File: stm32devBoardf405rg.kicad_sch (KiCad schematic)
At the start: 25 parts, among them Q1 AO3401A, SW1 SW_SPDT, U1 STM32F405RGT6, Y1 16MZ

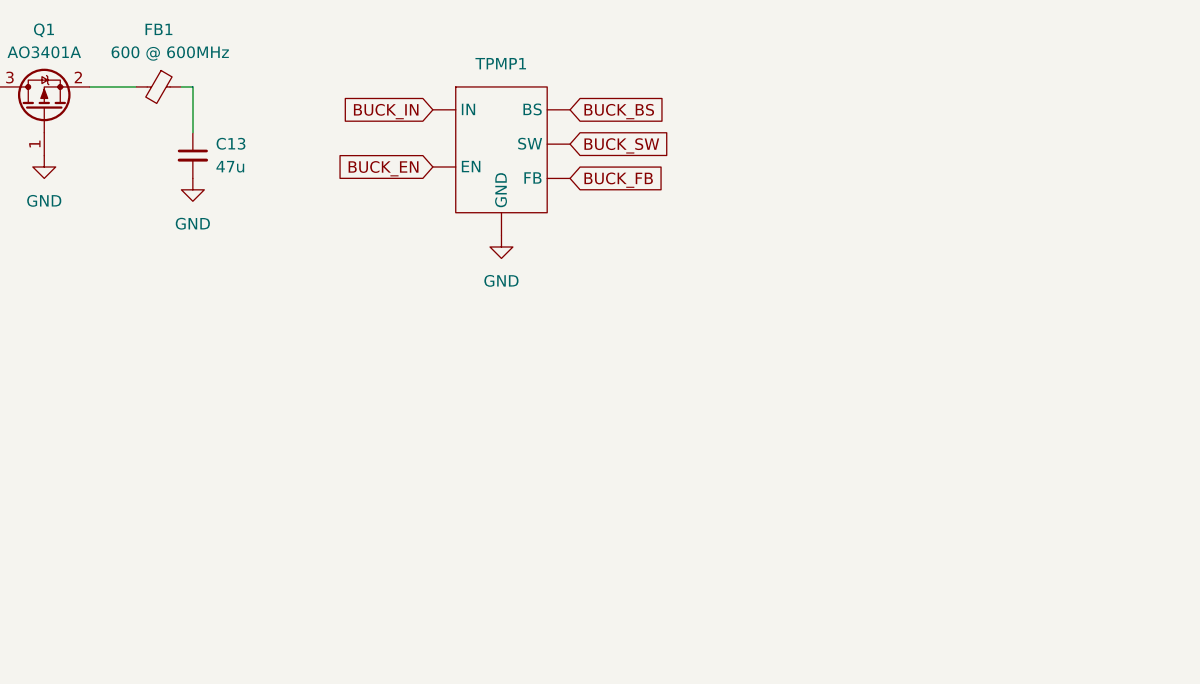
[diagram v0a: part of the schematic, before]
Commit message: added buck regulator TPMP2359 power supply
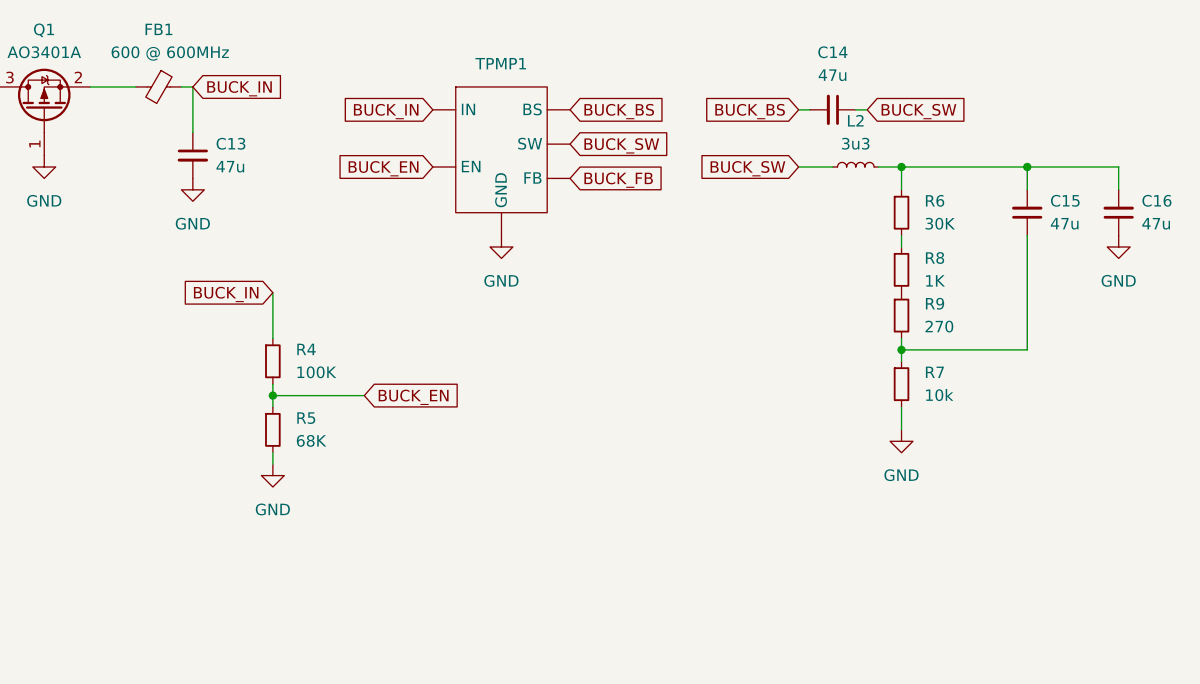
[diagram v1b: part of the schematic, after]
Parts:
- added C14, C15, C16: 47u, symbol Device:C_Small
- added L2: 3u3, symbol Device:L_Small
- added R4: 100K, symbol Device:R_Small
- added R5: 68K, symbol Device:R_Small
- added R6: 30K, symbol Device:R_Small
- added R7: 10k, symbol Device:R_Small
- added R8: 1K, symbol Device:R_Small
- added R9: 270, symbol Device:R_Small
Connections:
- net BUCK_BS: now also C14.2
- net BUCK_EN: now also R4.2, R5.1
- net BUCK_IN: now also C13.1, FB1.1, R4.1
- net BUCK_SW: now also C14.1, L2.1
- net GND: now also C16.1, R5.2, R7.2
- new net: C15.2, C16.2, L2.2, R6.1
- new net: R6.2, R8.1
- new net: R8.2, R9.1
- new net: C15.1, R7.1, R9.2

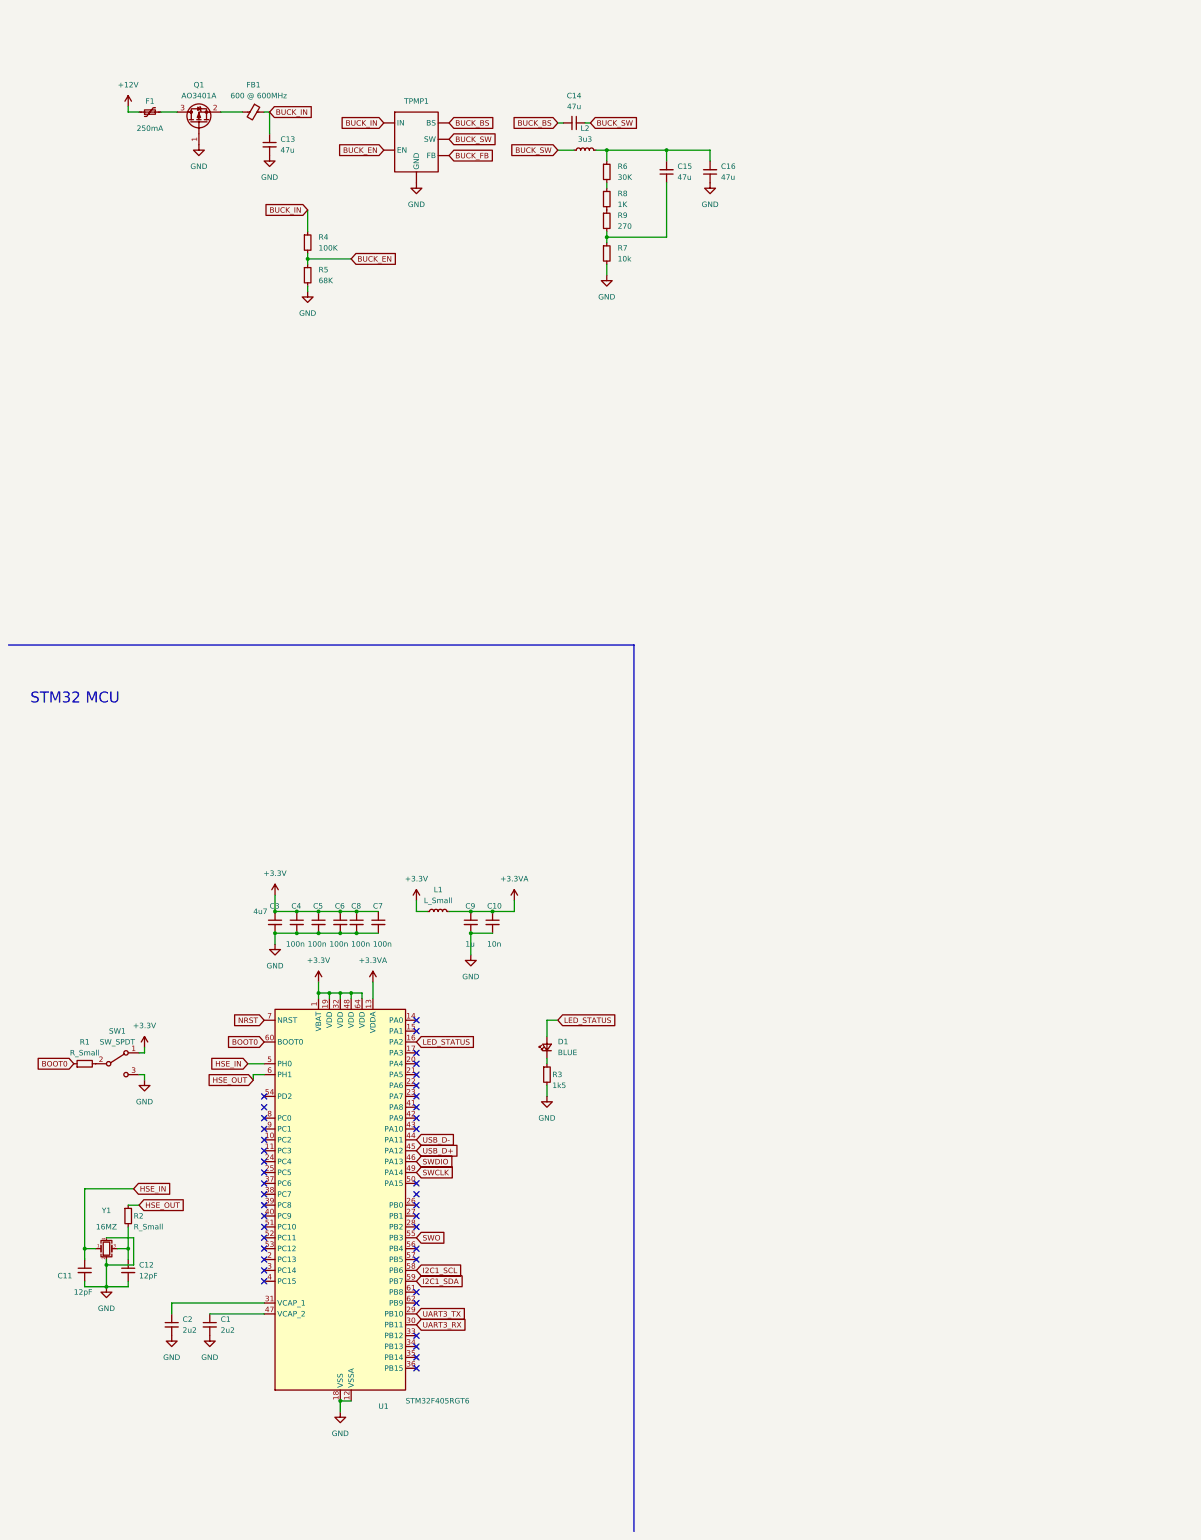
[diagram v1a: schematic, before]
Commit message: added I2C
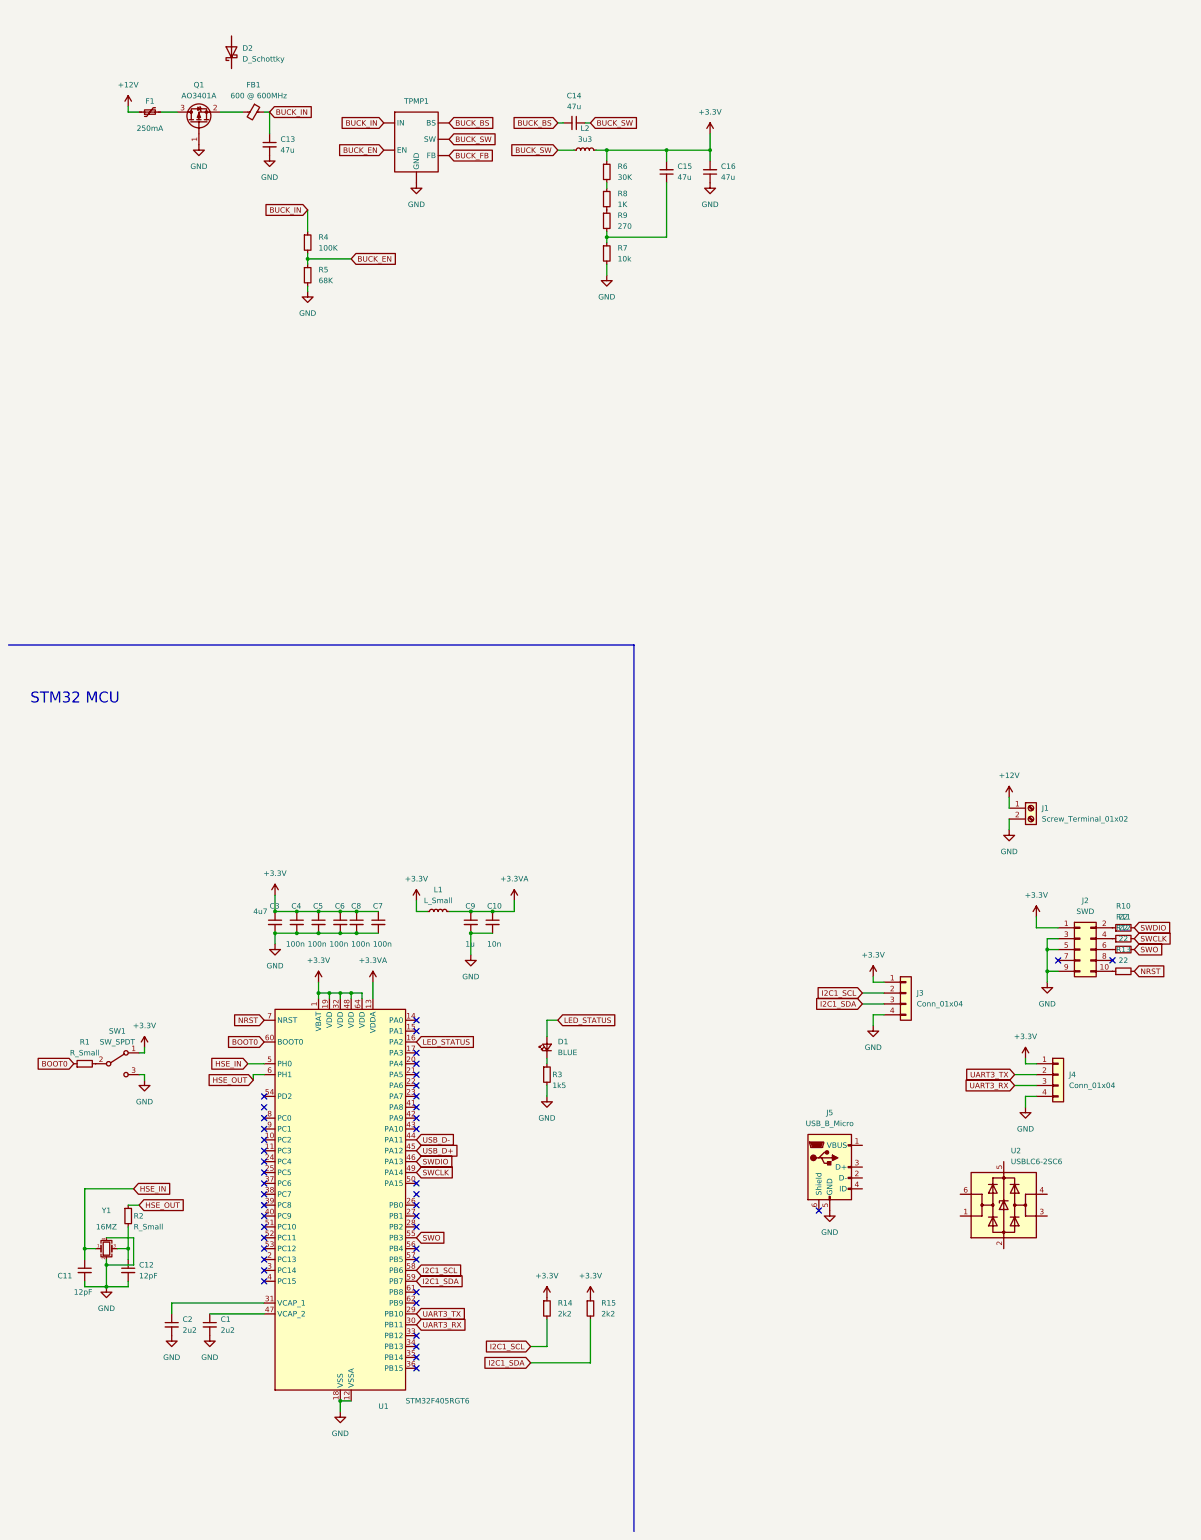
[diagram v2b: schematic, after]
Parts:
- added D2: D_Schottky, symbol Device:D_Schottky
- added J1: Screw_Terminal_01x02, symbol Connector:Screw_Terminal_01x02
- added J2: SWD, symbol Connector_Generic:Conn_02x05_Odd_Even
- added J3, J4: Conn_01x04, symbol Connector_Generic:Conn_01x04
- added J5: USB_B_Micro, symbol Connector:USB_B_Micro
- added R10, R11, R12, R13: 22, symbol Device:R_Small
- added R14, R15: 2k2, symbol Device:R_Small
- added U2: USBLC6-2SC6, Package_TO_SOT_SMD:SOT-23-6, symbol Power_Protection:USBLC6-2SC6
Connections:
- net +12V: now also J1.1 (Pin_1)
- net +3.3V: now also C15.2, C16.2, L2.2, R6.1, J2.1 (Pin_1), J3.1 (Pin_1), J4.1 (Pin_1), R14.1, R15.1
- net GND: now also J1.2 (Pin_2), J2.3 (Pin_3), J2.5 (Pin_5), J2.9 (Pin_9), J3.4 (Pin_4), J4.4 (Pin_4), J5.5 (GND)
- net I2C1_SCL: now also J3.2 (Pin_2), R14.2
- net I2C1_SDA: now also J3.3 (Pin_3), R15.2
- net NRST: now also R13.2
- net SWCLK: now also R11.2
- net SWDIO: now also R10.2
- net SWO: now also R12.2
- net UART3_RX: now also J4.3 (Pin_3)
- net UART3_TX: now also J4.2 (Pin_2)
- new net: J2.10 (Pin_10), R13.1
- new net: J2.2 (Pin_2), R10.1
- new net: J2.4 (Pin_4), R11.1
- new net: J2.6 (Pin_6), R12.1
- no-connect marks 41 -> 44
